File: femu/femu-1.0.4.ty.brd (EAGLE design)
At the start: 24.1 x 15.8 mm, 56 parts, among them IC1 ESP32-QFN_5X5

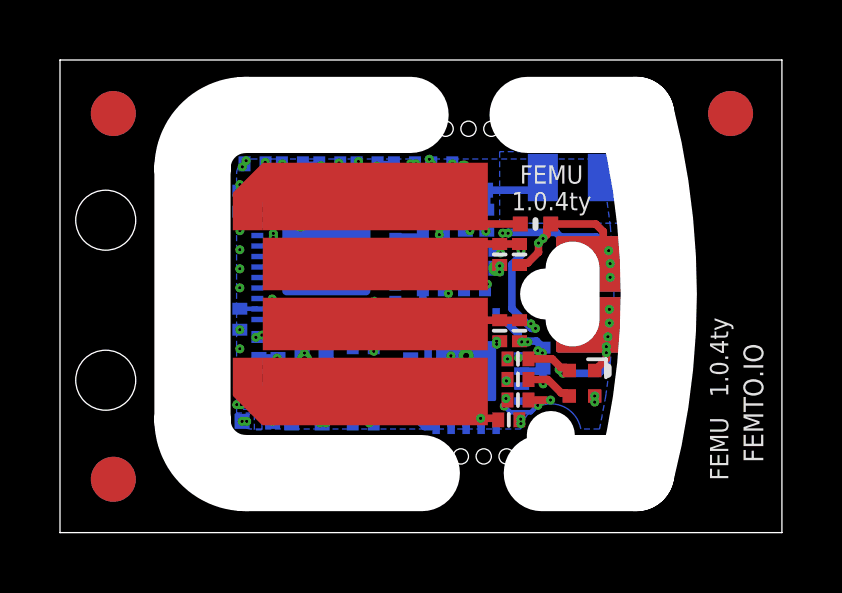
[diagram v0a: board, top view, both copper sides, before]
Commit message: Updating ground plane clearance, adding more ground plane vias, adjusting ground plane copper pour
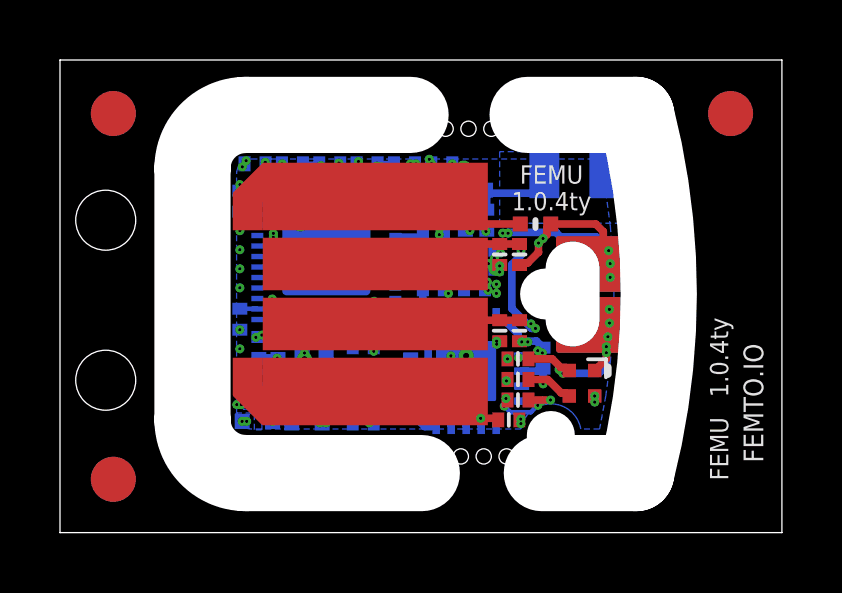
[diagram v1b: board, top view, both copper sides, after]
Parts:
- moved U$38 0.11 mm to (17.1, 11.9)
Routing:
- net GND: track 73.3 -> 71.4 mm, vias 92 -> 99

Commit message: Adjusted trace with of some RGB traces to 8mil, added more ground vias, connected ground pad under ESP32 using 5mil trace to other ground polygon area
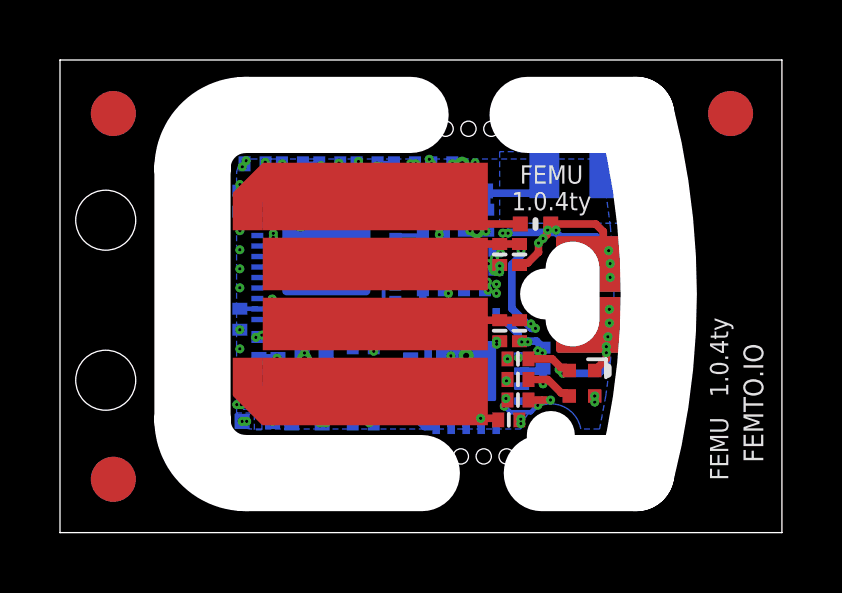
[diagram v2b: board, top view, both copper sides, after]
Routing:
- net GND: track 71.4 -> 75.7 mm, vias 99 -> 101

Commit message: Removing junk ftdi config (empty file), updating taydo-yuden-rf-antenna library with an experimental footprint. Adjusting ground plane and antenna trace of femu-1.0.4.ty design
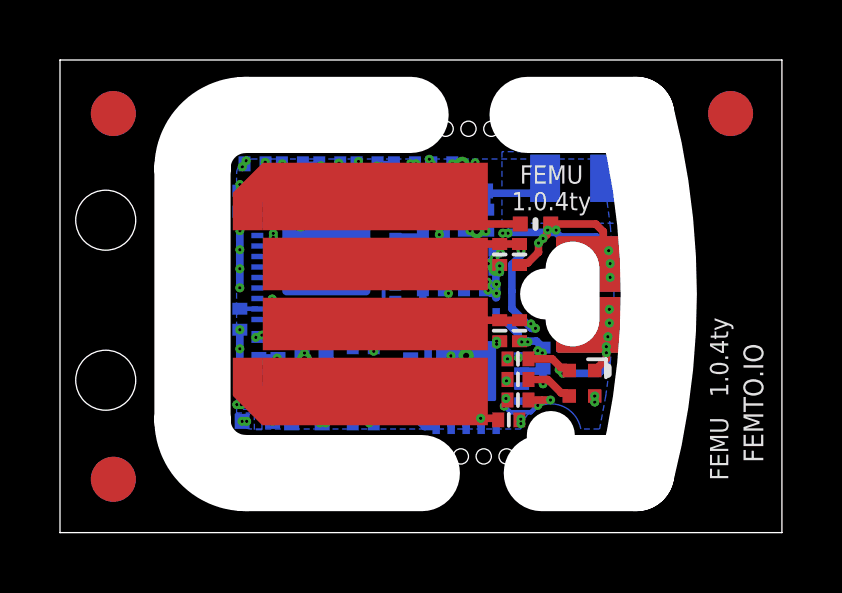
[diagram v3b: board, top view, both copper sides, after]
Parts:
- moved U$38 0.13 mm to (17.2, 11.8)
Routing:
- net GND: track 75.7 -> 90.4 mm
